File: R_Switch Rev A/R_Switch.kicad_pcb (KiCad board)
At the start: 2 copper layers, 78.7 x 92.7 mm, 137 parts, among them J1 Conn_01x04, J2 Conn_01x06, J3 Conn_01x06, J4 Conn_01x05, J5 Conn_01x08, J6 Conn_01x08, Q1 IRF7343PBF, Q2 IRF7343PBF, Q3 IRF7343PBF, Q4 IRF7343PBF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

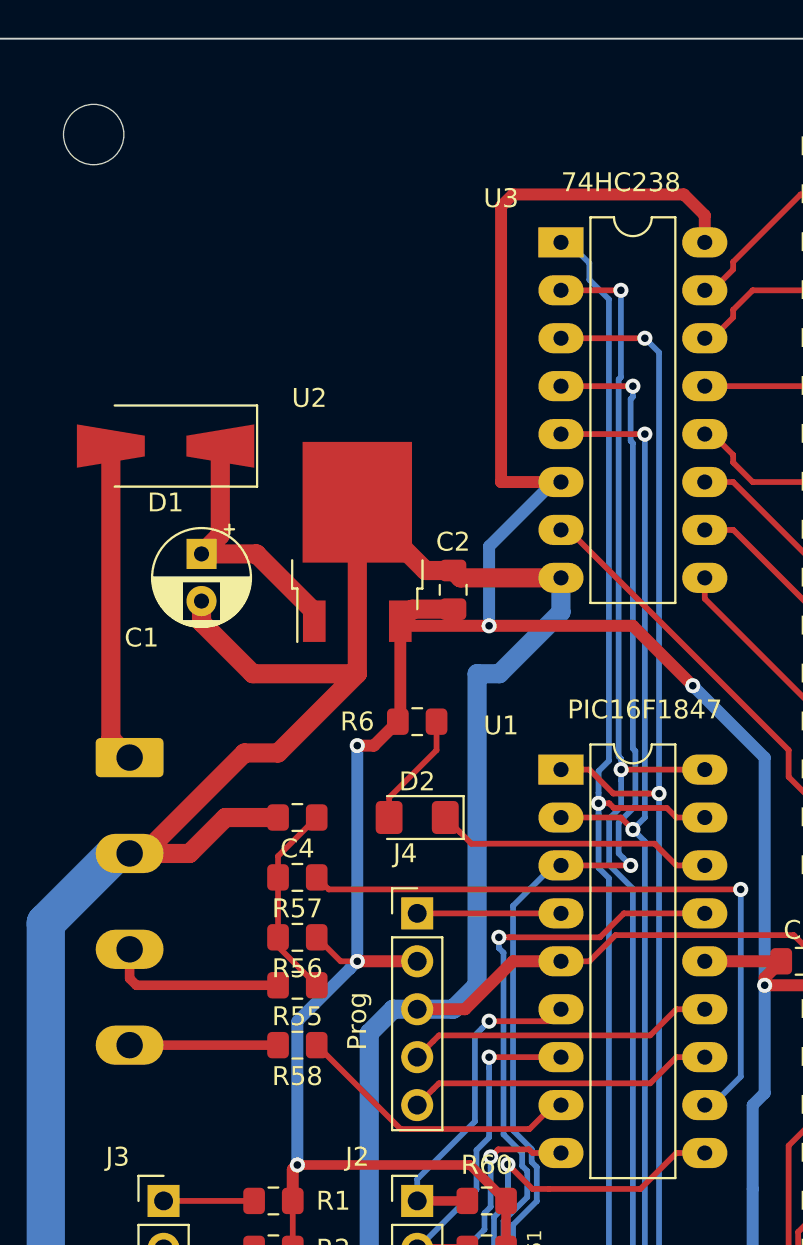
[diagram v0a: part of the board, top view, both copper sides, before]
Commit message: Enable and inhibit inputs
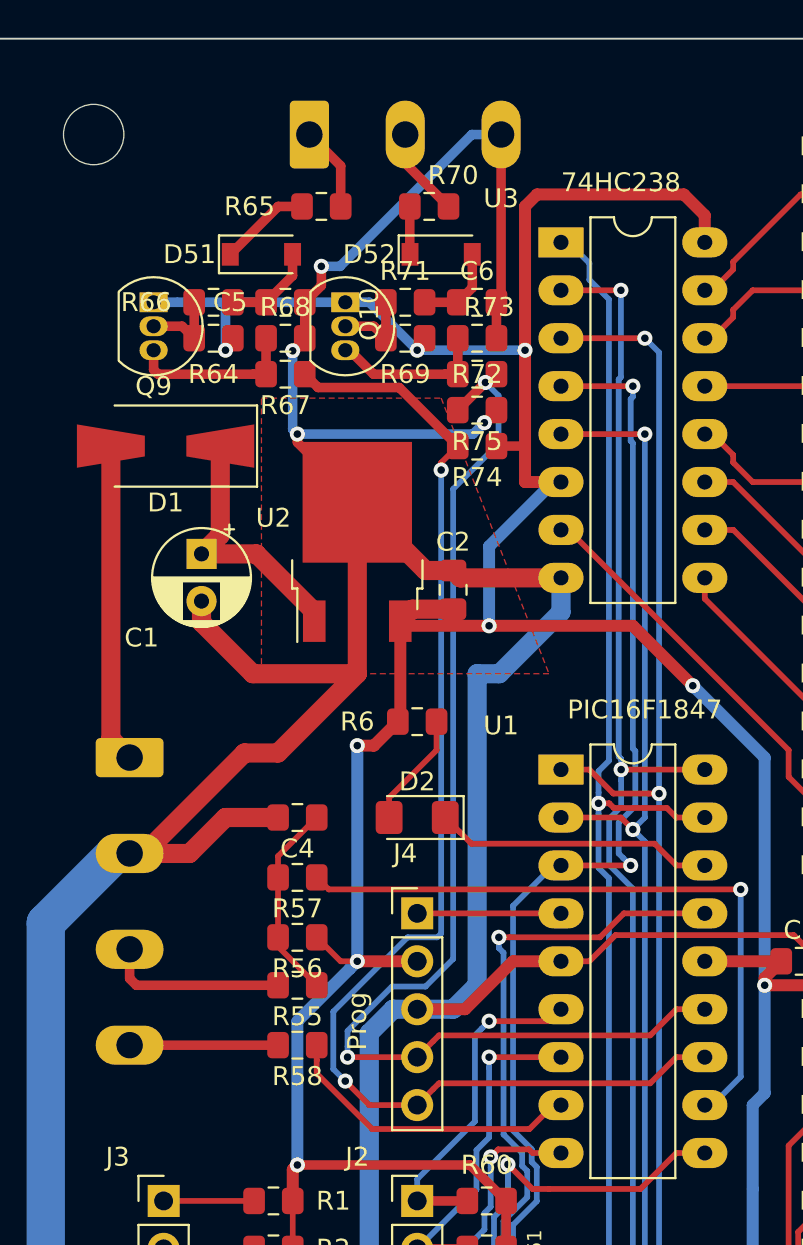
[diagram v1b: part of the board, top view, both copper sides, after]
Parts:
- added C5: 0.1, Capacitor_SMD:C_0805_2012Metric_Pad1.15x1.40mm_HandSolder, F.Cu at (94.0, 52.1)
- added C6: 0.1, Capacitor_SMD:C_0805_2012Metric_Pad1.15x1.40mm_HandSolder, F.Cu at (104.1, 52.1)
- added D51: D_Small_ALT, Diode_SMD:D_SOD-123, F.Cu at (92.7, 49.5)
- added D52: D_Small_ALT, Diode_SMD:D_SOD-123, F.Cu at (102.2, 49.5)
- added J7: Conn_01x03, Connector_Phoenix_MSTB:PhoenixContact_MSTBVA_2,5_3-G-5,08_1x03_P5.08mm_Vertical, B.Cu at (95.2, 43.2)
- added Q10: 2N3906, Package_TO_SOT_THT:TO-92_Inline, F.Cu at (97.2, 52.1)
- added Q9: 2N3906, Package_TO_SOT_THT:TO-92_Inline, F.Cu at (87.0, 52.1)
- added R64: 47K, Resistor_SMD:R_0805_2012Metric_Pad1.15x1.40mm_HandSolder, F.Cu at (90.2, 54.0)
- added R65: 1K0, Resistor_SMD:R_0805_2012Metric_Pad1.15x1.40mm_HandSolder, F.Cu at (95.9, 47.0)
- added R66: 10K, Resistor_SMD:R_0805_2012Metric_Pad1.15x1.40mm_HandSolder, F.Cu at (90.2, 52.1)
- added R67: 1K0, Resistor_SMD:R_0805_2012Metric_Pad1.15x1.40mm_HandSolder, F.Cu at (94.0, 55.9)
- added R68: 47K, Resistor_SMD:R_0805_2012Metric_Pad1.15x1.40mm_HandSolder, F.Cu at (94.0, 54.0)
- added R69: 47K, Resistor_SMD:R_0805_2012Metric_Pad1.15x1.40mm_HandSolder, F.Cu at (100.3, 54.0)
- added R70: 1K0, Resistor_SMD:R_0805_2012Metric_Pad1.15x1.40mm_HandSolder, F.Cu at (101.6, 47.0)
- added R71: 10K, Resistor_SMD:R_0805_2012Metric_Pad1.15x1.40mm_HandSolder, F.Cu at (100.3, 52.1)
- added R72: 1K0, Resistor_SMD:R_0805_2012Metric_Pad1.15x1.40mm_HandSolder, F.Cu at (104.1, 55.9)
- added R73: 47K, Resistor_SMD:R_0805_2012Metric_Pad1.15x1.40mm_HandSolder, F.Cu at (104.1, 54.0)
- added R74: 47K, Resistor_SMD:R_0805_2012Metric_Pad1.15x1.40mm_HandSolder, F.Cu at (104.1, 59.7)
- added R75: 47K, Resistor_SMD:R_0805_2012Metric_Pad1.15x1.40mm_HandSolder, F.Cu at (104.1, 57.8)
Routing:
- net PGC: track 16.3 -> 67.9 mm, vias 0 -> 2
- net GND: track 465.7 -> 514.7 mm, vias 16 -> 20
- net PGD: track 16.3 -> 63.2 mm, vias 0 -> 2
- net +5V: track 280.9 -> 304.8 mm, vias 6 -> 9
- net Net-(Q9-Pad3): track 0.00 -> 9.00 mm
- net Net-(Q10-Pad3): track 0.00 -> 8.39 mm
- net Net-(C5-Pad1): track 0.00 -> 4.88 mm
- net Net-(D51-Pad1): track 0.00 -> 4.85 mm
- net Net-(J7-Pad2): track 0.00 -> 4.76 mm
- net Net-(C6-Pad1): track 0.00 -> 4.62 mm
- net Net-(J7-Pad1): track 0.00 -> 4.50 mm
- net Net-(Q10-Pad2): track 0.00 -> 4.32 mm
- net Net-(Q9-Pad2): track 0.00 -> 4.32 mm
- net Net-(D52-Pad1): track 0.00 -> 2.54 mm
- net Net-(R58-Pad1): track 15.3 -> 16.2 mm
- added copper zone on F.Cu, net GND
